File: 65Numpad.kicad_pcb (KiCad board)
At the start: 2 copper layers, 137 parts, among them J1 MX-NoLED, K1 MX-NoLED, M1 MX-NoLED, P1 MX-NoLED, Q1 MX-NoLED, T1 MX-NoLED, U1 ProMicro, U2 MX-NoLED, X1 MX-NoLED, Y1 MX-NoLED

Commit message: Almost done routing
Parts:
- D1, D10, D11, D12, D13, D14, D15, D16, D17, D18, D19, D2, D20, D21, D22, D23, D24, D25, D26, D27, D28, D3, D30, D31, D32, D33, D34, D35, D36, D37, D38, D39, D4, D40, D41, D42, D43, D44, D45, D46, D47, D48, D49, D5, D50, D51, D52, D53, D54, D55, D56, D57, D58, D59, D6, D60, D61, D62, D63, D64, D65, D66, D67, D68, D7, D8, D9: moved to B.Cu
- moved D57 38.1 mm to (295.3, 85.7)
- moved D43 38.1 mm to (295.3, 66.7)
- moved D67 38.1 mm to (295.3, 104.8)
- moved D68 38.1 mm to (295.3, 123.8)
- moved U1 32.6 mm to (14.3, 96.8), turned to 0 degrees
- moved POGO1 16.9 mm to (0.00, 81.8)
- moved POGO2 11.8 mm to (299.2, 73.8)
- moved D36 5.07 mm to (142.1, 102.1), turned to 90 degrees
- moved D41 5.07 mm to (237.3, 102.1), turned to 90 degrees
- moved D52 5.07 mm to (189.7, 121.1), turned to 90 degrees
- moved D25 5.07 mm to (213.5, 83.0), turned to 90 degrees
- moved D33 5.07 mm to (84.9, 102.1), turned to 90 degrees
- moved D34 5.07 mm to (104.0, 102.1), turned to 90 degrees
- moved D6 5.07 mm to (108.7, 64.0), turned to 90 degrees
- moved D7 5.07 mm to (127.8, 64.0), turned to 90 degrees
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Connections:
- U1 pad 1: ROW0 -> ROW6
- U1 pad 10: ROW6 -> COL4
- U1 pad 11: ROW7 -> COL5
- U1 pad 12: ROW8 -> COL6
- U1 pad 13: COL6 -> ROW5
- U1 pad 14: COL5 -> ROW4
- U1 pad 15: COL4 -> COL1
- U1 pad 16: COL3 -> ROW3
- U1 pad 17: COL2 -> ROW2
- U1 pad 18: COL1 -> ROW1
- U1 pad 19: COL0 -> ROW0
- U1 pad 20: ROW9 -> COL0
- U1 pad 23: (no net) -> GND
- U1 pad 5: ROW1 -> ROW7
- U1 pad 6: ROW2 -> COL2
- U1 pad 7: ROW3 -> COL3
- U1 pad 8: ROW4 -> ROW8
- U1 pad 9: ROW5 -> ROW9
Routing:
- net COL4: track 0.00 -> 503.0 mm, vias 0 -> 19
- net COL2: track 0.00 -> 502.1 mm, vias 0 -> 16
- net COL3: track 0.00 -> 462.1 mm, vias 0 -> 24
- net COL6: track 0.00 -> 453.7 mm, vias 0 -> 18
- net COL5: track 0.00 -> 447.9 mm, vias 0 -> 16
- net ROW8: track 0.00 -> 365.6 mm
- net ROW9: track 0.00 -> 343.6 mm, vias 0 -> 6
- net ROW7: track 0.00 -> 340.5 mm, vias 0 -> 12
- net ROW6: track 0.00 -> 320.6 mm
- net COL1: track 0.00 -> 317.2 mm, vias 0 -> 16
- net ROW5: track 0.00 -> 308.2 mm, vias 0 -> 10
- net ROW1: track 0.00 -> 291.0 mm, vias 0 -> 12
- net ROW4: track 0.00 -> 287.1 mm
- net ROW0: track 0.00 -> 276.0 mm, vias 0 -> 2
- net ROW3: track 0.00 -> 272.9 mm, vias 0 -> 12
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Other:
- net class Default: trace_width 0.25 -> 0.254
- net class Power added: clearance 0.2, trace_width 0.381, via_dia 0.8, via_drill 0.4

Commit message: Finished routing
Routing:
- net SERIAL: track 26.4 -> 359.4 mm, vias 0 -> 7
- net GND: track 13.7 -> 344.0 mm, vias 0 -> 6
- net VCC: track 19.5 -> 345.7 mm, vias 0 -> 7
- net COL5: track 447.9 -> 438.4 mm, vias 16 -> 14
- net COL4: track 503.0 -> 495.1 mm, vias 19 -> 17
- net COL6: track 453.7 -> 452.7 mm, vias 18 -> 12
- net ROW8: track 365.6 -> 366.4 mm
- net COL3: vias 24 -> 23

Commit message: Routed numpad
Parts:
- removed U1: ProMicro, Keebio-Parts:ArduinoProMicro
- added ASTERISK1: MX-NoLED, MX_Only:MXOnly-1U-NoLEDHotswap, F.Cu at (377.0, 58.7)
- added D69: 1N4148, Diodes_THT:D_DO-35_SOD27_P7.62mm_Horizontal, B.Cu at (342.9, 66.7)
- added D70: 1N4148, Diodes_THT:D_DO-35_SOD27_P7.62mm_Horizontal, B.Cu at (361.9, 66.7)
- added D71: 1N4148, Diodes_THT:D_DO-35_SOD27_P7.62mm_Horizontal, B.Cu at (381.0, 66.7)
- added D72: 1N4148, Diodes_THT:D_DO-35_SOD27_P7.62mm_Horizontal, B.Cu at (400.1, 66.7)
- added D73: 1N4148, Diodes_THT:D_DO-35_SOD27_P7.62mm_Horizontal, B.Cu at (342.9, 85.7)
- added D74: 1N4148, Diodes_THT:D_DO-35_SOD27_P7.62mm_Horizontal, B.Cu at (361.9, 85.7)
- added D75: 1N4148, Diodes_THT:D_DO-35_SOD27_P7.62mm_Horizontal, B.Cu at (381.0, 85.7)
- added D76: 1N4148, Diodes_THT:D_DO-35_SOD27_P7.62mm_Horizontal, B.Cu at (342.9, 104.8)
- added D77: 1N4148, Diodes_THT:D_DO-35_SOD27_P7.62mm_Horizontal, B.Cu at (361.9, 104.8)
- added D78: 1N4148, Diodes_THT:D_DO-35_SOD27_P7.62mm_Horizontal, B.Cu at (381.0, 104.8)
- added D79: 1N4148, Diodes_THT:D_DO-35_SOD27_P7.62mm_Horizontal, B.Cu at (400.1, 95.2)
- added D80: 1N4148, Diodes_THT:D_DO-35_SOD27_P7.62mm_Horizontal, B.Cu at (342.9, 123.8)
- added D81: 1N4148, Diodes_THT:D_DO-35_SOD27_P7.62mm_Horizontal, B.Cu at (361.9, 123.8)
- added D82: 1N4148, Diodes_THT:D_DO-35_SOD27_P7.62mm_Horizontal, B.Cu at (381.0, 123.8)
- added D83: 1N4148, Diodes_THT:D_DO-35_SOD27_P7.62mm_Horizontal, B.Cu at (352.4, 142.9)
- added D84: 1N4148, Diodes_THT:D_DO-35_SOD27_P7.62mm_Horizontal, B.Cu at (381.0, 142.9)
- added D85: 1N4148, Diodes_THT:D_DO-35_SOD27_P7.62mm_Horizontal, B.Cu at (400.1, 133.3)
- added DEL2: MX-NoLED, MX_Only:MXOnly-1U-NoLEDHotswap, F.Cu at (377.0, 134.9)
- added EIGHT2: MX-NoLED, MX_Only:MXOnly-1U-NoLEDHotswap, F.Cu at (358.0, 77.8)
- added ENTER2: MX-NoLED, MX_Only:MXOnly-2U-NoLEDHotswap, F.Cu at (396.1, 125.4)
- added FIVE2: MX-NoLED, MX_Only:MXOnly-1U-NoLEDHotswap, F.Cu at (358.0, 96.8)
- added FOUR2: MX-NoLED, MX_Only:MXOnly-1U-NoLEDHotswap, F.Cu at (338.9, 96.8)
- added MINUS2: MX-NoLED, MX_Only:MXOnly-1U-NoLEDHotswap, F.Cu at (396.1, 58.7)
- added Main1: ProMicro, Keebio-Parts:ArduinoProMicro, F.Cu at (12.7, 96.8)
- added NINE2: MX-NoLED, MX_Only:MXOnly-1U-NoLEDHotswap, F.Cu at (377.0, 77.8)
- added NUM1: MX-NoLED, MX_Only:MXOnly-1U-NoLEDHotswap, F.Cu at (338.9, 58.7)
- added Numpad1: ProMicro, Keebio-Parts:ArduinoProMicro, F.Cu at (358.0, 67.5)
- added ONE2: MX-NoLED, MX_Only:MXOnly-1U-NoLEDHotswap, F.Cu at (338.9, 115.9)
- added PLUS1: MX-NoLED, MX_Only:MXOnly-2U-NoLEDHotswap, F.Cu at (396.1, 87.3)
- added POGO3: Conn_01x04, Pin_Headers:Pin_Header_Angled_1x04_Pitch2.54mm, F.Cu at (326.7, 59.4)
- added POGO4: Conn_01x04, Pin_Headers:Pin_Header_Angled_1x04_Pitch2.54mm, F.Cu at (403.2, 55.6)
- added SEVEN2: MX-NoLED, MX_Only:MXOnly-1U-NoLEDHotswap, F.Cu at (338.9, 77.8)
- added SIX2: MX-NoLED, MX_Only:MXOnly-1U-NoLEDHotswap, F.Cu at (377.0, 96.8)
- added SLASH2: MX-NoLED, MX_Only:MXOnly-1U-NoLEDHotswap, F.Cu at (358.0, 58.7)
- added THREE2: MX-NoLED, MX_Only:MXOnly-1U-NoLEDHotswap, F.Cu at (377.0, 115.9)
- added TWO2: MX-NoLED, MX_Only:MXOnly-1U-NoLEDHotswap, F.Cu at (358.0, 115.9)
- added ZERO2: MX-NoLED, MX_Only:MXOnly-2U-NoLEDHotswap, F.Cu at (348.5, 134.9)
- moved POGO1 23.4 mm to (-6.67, 59.4), turned to 0 degrees
- moved POGO2 18.3 mm to (298.4, 55.6)
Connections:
- POGO1 pad 1: (no net) -> SERIAL
- POGO1 pad 2: SERIAL -> (no net)
- POGO2 pad 1: (no net) -> SERIAL
- POGO2 pad 2: SERIAL -> (no net)
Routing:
- net COL0: track 268.5 -> 398.4 mm
- net ROW4: track 287.1 -> 415.7 mm
- net SERIAL: track 359.4 -> 486.5 mm
- net COL3: track 462.1 -> 588.4 mm, vias 23 -> 24
- net GND: track 344.0 -> 460.6 mm, vias 6 -> 10
- net VCC: track 345.7 -> 456.2 mm, vias 7 -> 12
- net ROW2: track 265.0 -> 370.5 mm
- net COL1: track 317.2 -> 418.5 mm
- net ROW3: track 272.9 -> 370.7 mm, vias 12 -> 13
- net ROW1: track 291.0 -> 356.0 mm
- net ROW0: track 276.0 -> 339.9 mm
- net COL2: track 502.1 -> 540.2 mm, vias 16 -> 12
- net Net-(D69-Pad2): track 0.00 -> 16.6 mm
- net Net-(ASTERISK1-Pad2): track 0.00 -> 16.6 mm
- net Net-(D84-Pad2): track 0.00 -> 16.5 mm
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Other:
- board outline added: 304.8 x 95.3 mm

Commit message: Changed footprint to double sided hot swap
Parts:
- moved POGO3 6.35 mm to (331.8, 55.6)
- moved POGO1 6.35 mm to (-1.59, 55.6)
- moved Numpad1 1.11 mm to (358.0, 66.4)
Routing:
- net SERIAL: track 486.5 -> 492.2 mm
- net VCC: track 456.2 -> 459.0 mm
- net ROW0: track 339.9 -> 341.0 mm
- net ROW3: track 370.7 -> 371.8 mm
- net ROW1: track 356.0 -> 357.1 mm
- net ROW2: track 370.5 -> 371.6 mm
- net ROW4: track 415.7 -> 416.8 mm
- net COL0: track 398.4 -> 397.8 mm
- net GND: track 460.6 -> 460.1 mm
- net COL3: track 588.4 -> 588.9 mm, vias 24 -> 22
- net COL1: track 418.5 -> 418.7 mm, vias 16 -> 12
- net COL2: vias 12 -> 10
- net COL5: vias 16 -> 14
- net COL4: vias 19 -> 17
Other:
- board size 304.8 x 95.3 mm -> 412.8 x 98.4 mm

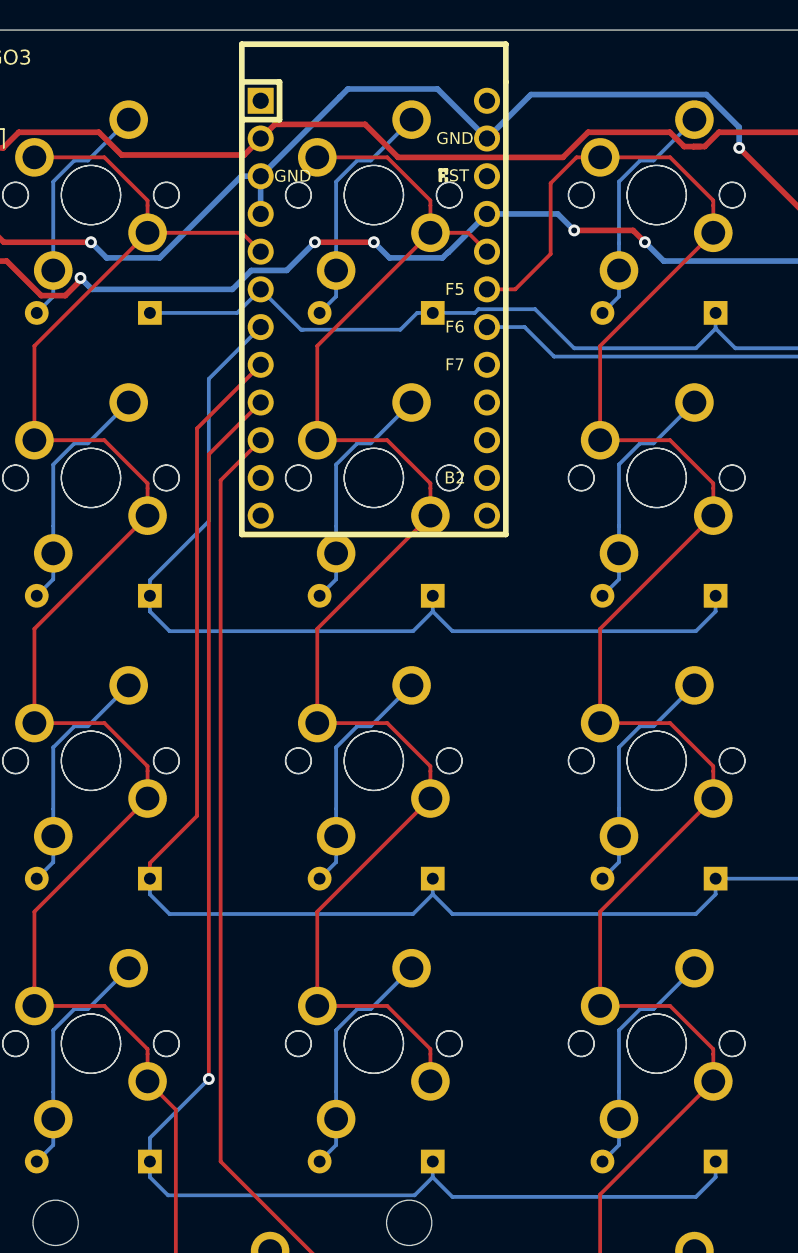
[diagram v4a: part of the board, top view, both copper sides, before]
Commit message: Adjusted positions
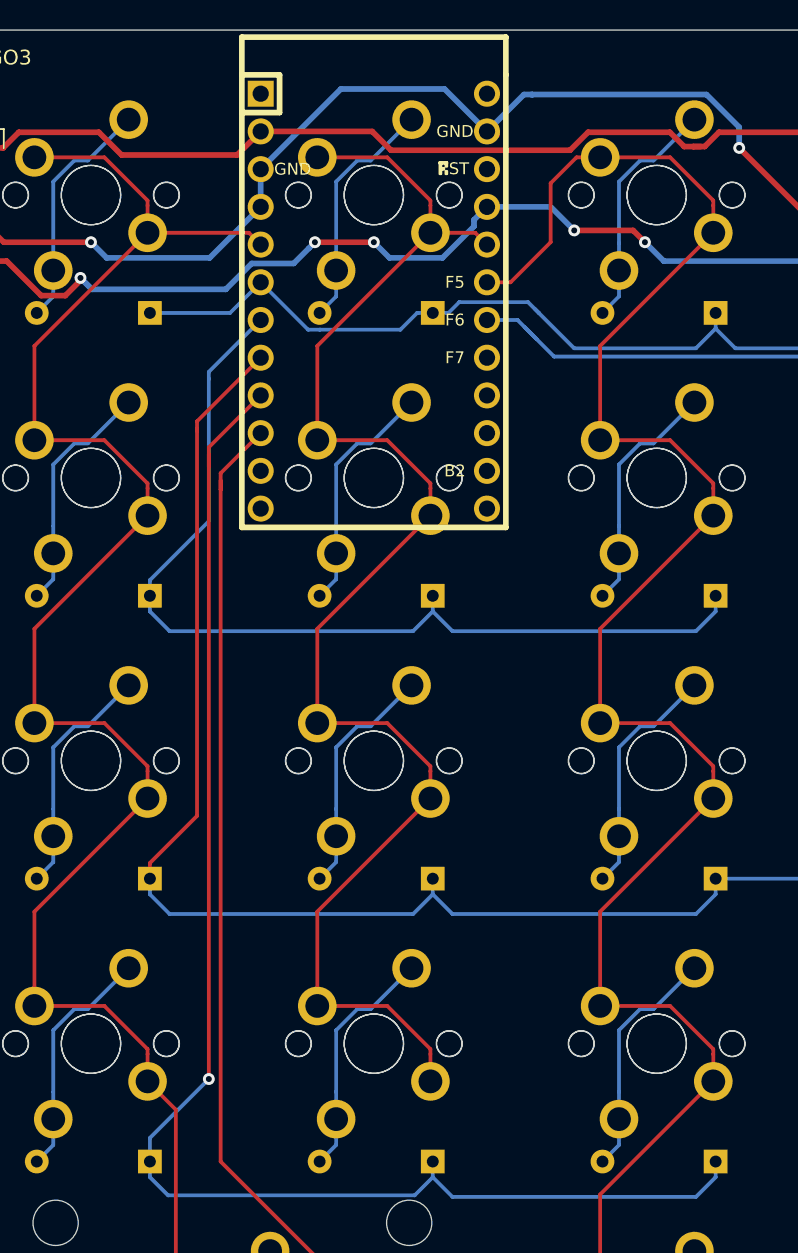
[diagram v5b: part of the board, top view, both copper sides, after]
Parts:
- moved Numpad1 0.48 mm to (358.0, 65.9)
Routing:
- net GND: track 460.1 -> 458.8 mm
- net COL3: track 588.9 -> 590.2 mm
- net ROW3: track 371.8 -> 373.1 mm
- net ROW0: track 341.0 -> 342.1 mm
- net ROW4: track 416.8 -> 417.9 mm
- net SERIAL: track 492.2 -> 491.4 mm
- net COL2: track 540.2 -> 539.5 mm
- net VCC: track 459.0 -> 459.7 mm
- net ROW2: track 371.6 -> 372.2 mm
